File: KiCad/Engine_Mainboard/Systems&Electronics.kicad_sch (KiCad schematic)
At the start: 50 parts, among them J1 Pressure Transducer, J12 Screw_Terminal_01x02, J13 Screw_Terminal_01x03, J2 Pressure Transducer, J3 Pressure Transducer, J4 Pressure Transducer, J5 Pressure Transducer, J6 Pressure Transducer

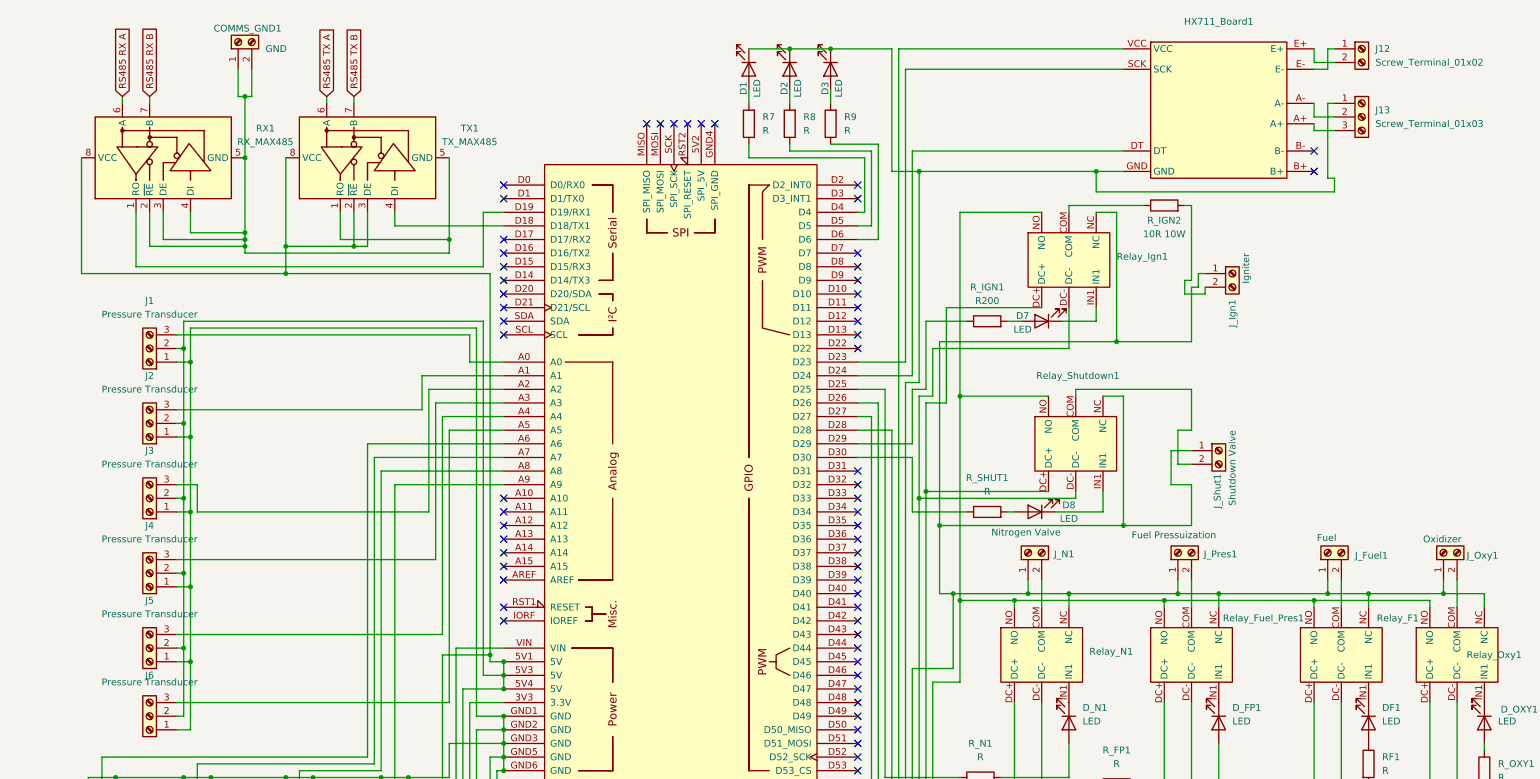
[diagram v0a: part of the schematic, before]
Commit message: PCB design reorg
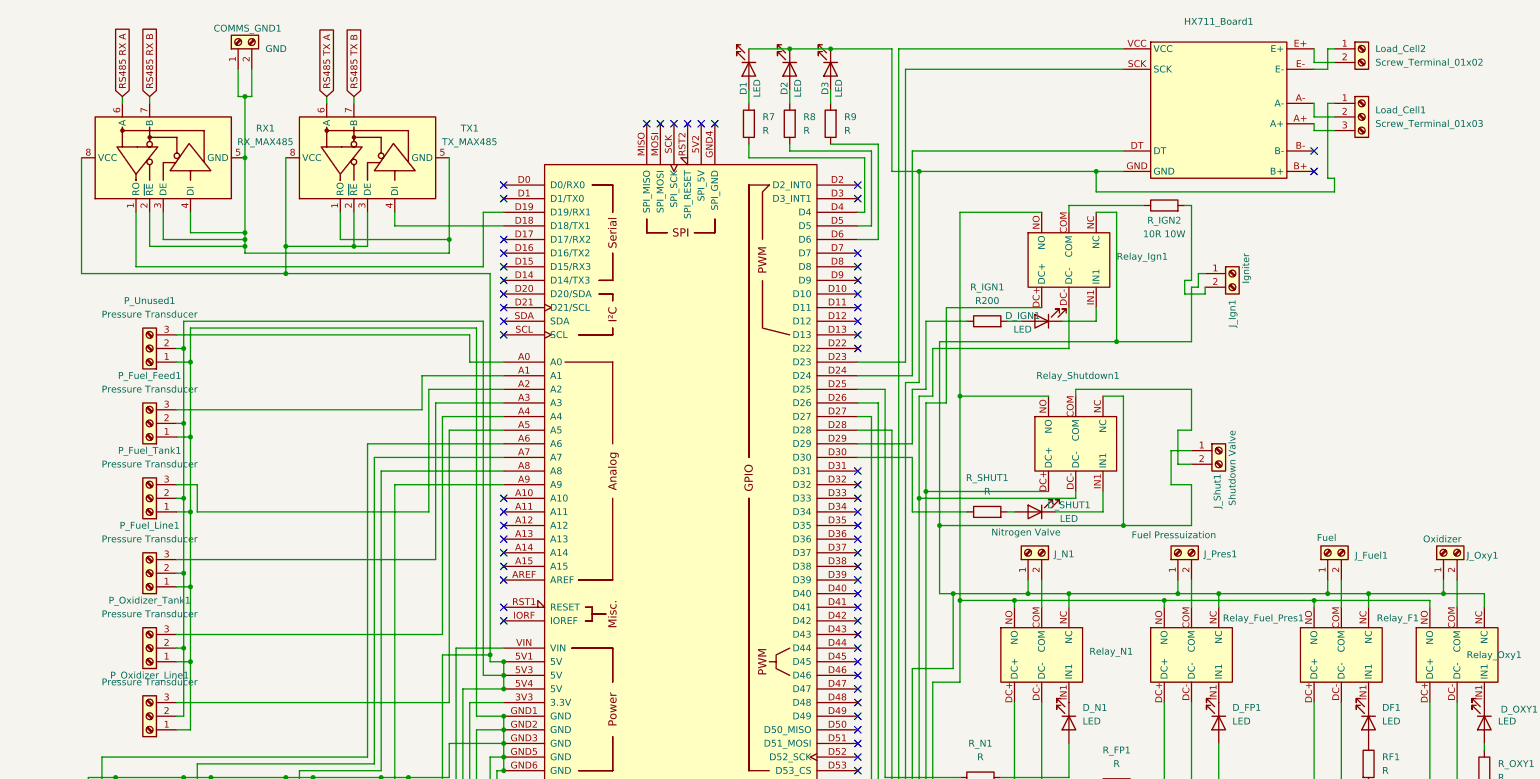
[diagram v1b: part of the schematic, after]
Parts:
- renumbered D7 to D_IGN1, D8 to D_SHUT1, J13 to Load_Cell1, J12 to Load_Cell2, J2 to P_Fuel_Feed1, J4 to P_Fuel_Line1, J3 to P_Fuel_Tank1, J6 to P_Oxidizer_Line1, J5 to P_Oxidizer_Tank1, J1 to P_Unused1
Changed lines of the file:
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@@
 		(on_board yes)
 		(dnp no)
-		(property "Reference" "J6"
+		(property "Reference" "P_Oxidizer_Line1"
 			(at 27.94 135.89 0)
 			(effects
@@
 			(project "Systems&Electronics"
 				(path "/4e05caf8-77e4-4a22-9a05-51fcca8e50ff"
-					(reference "J6")
+					(reference "P_Oxidizer_Line1")
 					(unit 1)
 				)
@@
 		(dnp no)
 		(fields_autoplaced yes)
-		(property "Reference" "J4"
+		(property "Reference" "P_Fuel_Line1"
 			(at 27.94 107.95 0)
 			(effects
@@
 			(project "Systems&Electronics"
 				(path "/4e05caf8-77e4-4a22-9a05-51fcca8e50ff"
-					(reference "J4")
+					(reference "P_Fuel_Line1")
 					(unit 1)
 				)
@@
 		(dnp no)
 		(fields_autoplaced yes)
-		(property "Reference" "J3"
+		(property "Reference" "P_Fuel_Tank1"
 			(at 27.94 93.98 0)
 			(effects
@@
 			(project "Systems&Electronics"
 				(path "/4e05caf8-77e4-4a22-9a05-51fcca8e50ff"
-					(reference "J3")
+					(reference "P_Fuel_Tank1")
 					(unit 1)
 				)
@@
 		(on_board yes)
 		(dnp no)
-		(property "Reference" "D8"
+		(property "Reference" "D_SHUT1"
 			(at 199.39 104.14 0)
 			(effects
@@
 			(project "Systems&Electronics"
 				(path "/4e05caf8-77e4-4a22-9a05-51fcca8e50ff"
-					(reference "D8")
+					(reference "D_SHUT1")
 					(unit 1)
 				)
@@
 	)
 	(symbol
+		(lib_name "Sensors:AD8495_PCB")
 		(lib_id "Sensors:AD8495_PCB")
 		(at 57.15 168.91 180)
@@
 	)
 	(symbol
+		(lib_name "Sensors:AD8495_PCB")
 		(lib_id "Sensors:AD8495_PCB")
 		(at 74.93 168.91 180)
@@
 		(dnp no)
 		(fields_autoplaced yes)
-		(property "Reference" "J2"
+		(property "Reference" "P_Fuel_Feed1"
 			(at 27.94 80.01 0)
 			(effects
@@
 			(project ""
 				(path "/4e05caf8-77e4-4a22-9a05-51fcca8e50ff"
-					(reference "J2")
+					(reference "P_Fuel_Feed1")
 					(unit 1)
 				)
@@
 		(dnp no)
 		(fields_autoplaced yes)
-		(property "Reference" "J12"
+		(property "Reference" "Load_Cell2"
 			(at 256.54 19.0499 0)
 			(effects
@@
 			(project ""
 				(path "/4e05caf8-77e4-4a22-9a05-51fcca8e50ff"
-					(reference "J12")
+					(reference "Load_Cell2")
 					(unit 1)
 				)
@@
 		(dnp no)
 		(fields_autoplaced yes)
-		(property "Reference" "J1"
+		(property "Reference" "P_Unused1"
 			(at 27.94 66.04 0)
 			(effects
@@
 			(project "Systems&Electronics"
 				(path "/4e05caf8-77e4-4a22-9a05-51fcca8e50ff"
-					(reference "J1")
+					(reference "P_Unused1")
 					(unit 1)
 				)
@@
 	)
 	(symbol
+		(lib_name "Sensors:AD8495_PCB")
 		(lib_id "Sensors:AD8495_PCB")
 		(at 38.1 168.91 180)
@@
 		(dnp no)
 		(fields_autoplaced yes)
-		(property "Reference" "J13"
+		(property "Reference" "Load_Cell1"
 			(at 256.54 30.4799 0)
 			(effects
@@
 			(project ""
 				(path "/4e05caf8-77e4-4a22-9a05-51fcca8e50ff"
-					(reference "J13")
+					(reference "Load_Cell1")
 					(unit 1)
 				)
@@
 		(dnp no)
 		(fields_autoplaced yes)
-		(property "Reference" "J5"
+		(property "Reference" "P_Oxidizer_Tank1"
 			(at 27.94 121.92 0)
 			(effects
@@
 			(project "Systems&Electronics"
 				(path "/4e05caf8-77e4-4a22-9a05-51fcca8e50ff"
-					(reference "J5")
+					(reference "P_Oxidizer_Tank1")
 					(unit 1)
 				)
@@
 	)
 	(symbol
+		(lib_name "Sensors:AD8495_PCB")
 		(lib_id "Sensors:AD8495_PCB")
 		(at 20.32 168.91 180)
@@
 		(on_board yes)
 		(dnp no)
-		(property "Reference" "D7"
+		(property "Reference" "D_IGN1"
 			(at 190.754 68.834 0)
 			(effects
@@
 			(project "Systems&Electronics"
 				(path "/4e05caf8-77e4-4a22-9a05-51fcca8e50ff"
-					(reference "D7")
+					(reference "D_IGN1")
 					(unit 1)
 				)

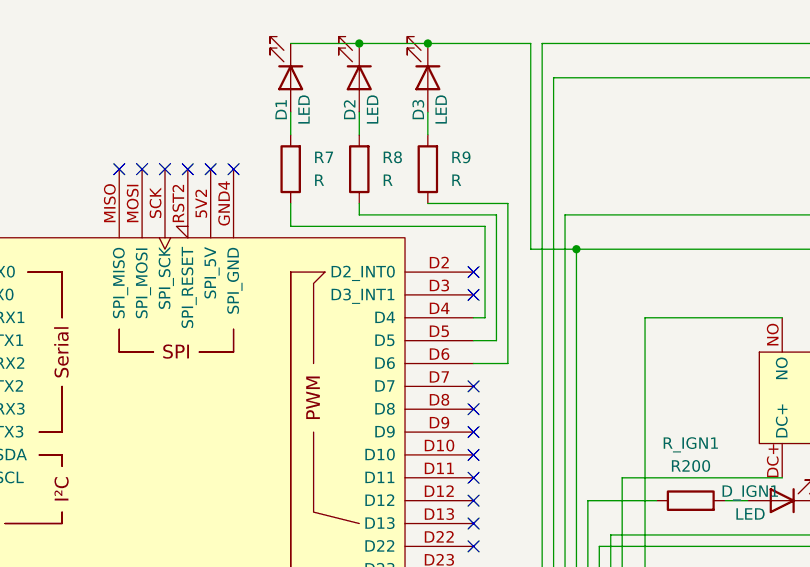
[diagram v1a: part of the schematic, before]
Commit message: PCB Ignition Resistor Move
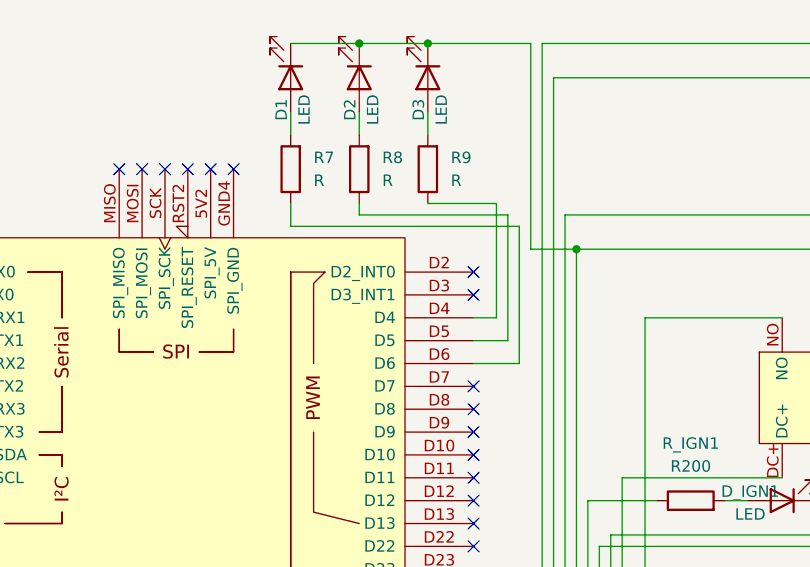
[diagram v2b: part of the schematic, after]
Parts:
- D1, D2, D3, DF1, D_FP1, D_IGN1, D_N1, D_OXY1, D_SHUT1: footprint LED_THT:LED_D3.0mm -> LED_THT:LED_D5.0mm
- R7, R8, R9, RF1, R_FP1, R_IGN1, R_N1, R_OXY1, R_SHUT1: footprint Resistor_THT:R_Axial_DIN0204_L3.6mm_D1.6mm_P5.08mm_Horizontal -> Resistor_THT:R_Axial_DIN0207_L6.3mm_D2.5mm_P7.62mm_Horizontal
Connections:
- net at R9.1: now also A1.D4; no longer A1.D6
- net at R7.1: now also A1.D6; no longer A1.D4
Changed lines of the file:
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@@
 	(wire
 		(pts
+			(xy 163.83 38.1) (xy 163.83 52.07)
+		)
+		(stroke
+			(width 0)
+			(type default)
+		)
+	)
+	(wire
+		(pts
 			(xy 36.83 152.4) (xy 36.83 160.02)
 		)
@@
 	(wire
 		(pts
-			(xy 161.29 39.37) (xy 161.29 49.53)
-		)
-		(stroke
-			(width 0)
-			(type default)
-		)
-	)
-	(wire
-		(pts
 			(xy 199.39 148.59) (xy 199.39 154.94)
 		)
@@
 	(wire
 		(pts
-			(xy 160.02 52.07) (xy 162.56 52.07)
+			(xy 160.02 52.07) (xy 163.83 52.07)
 		)
 		(stroke
@@
 	(wire
 		(pts
-			(xy 162.56 38.1) (xy 147.32 38.1)
+			(xy 147.32 38.1) (xy 163.83 38.1)
 		)
 		(stroke
@@
 	(wire
 		(pts
-			(xy 163.83 54.61) (xy 163.83 36.83)
-		)
-		(stroke
-			(width 0)
-			(type default)
-		)
-	)
-	(wire
-		(pts
 			(xy 208.28 49.53) (xy 208.28 73.66)
 		)
@@
 	(wire
 		(pts
+			(xy 162.56 36.83) (xy 162.56 49.53)
+		)
+		(stroke
+			(width 0)
+			(type default)
+		)
+	)
+	(wire
+		(pts
 			(xy 53.34 39.37) (xy 53.34 55.88)
 		)
@@
 	(wire
 		(pts
-			(xy 160.02 54.61) (xy 163.83 54.61)
+			(xy 160.02 54.61) (xy 165.1 54.61)
 		)
 		(stroke
@@
 	(wire
 		(pts
+			(xy 162.56 36.83) (xy 154.94 36.83)
+		)
+		(stroke
+			(width 0)
+			(type default)
+		)
+	)
+	(wire
+		(pts
 			(xy 90.17 135.89) (xy 93.98 135.89)
 		)
@@
 	(wire
 		(pts
-			(xy 162.56 52.07) (xy 162.56 38.1)
-		)
-		(stroke
-			(width 0)
-			(type default)
-		)
-	)
-	(wire
-		(pts
 			(xy 250.19 118.11) (xy 250.19 123.19)
 		)
@@
 	(wire
 		(pts
-			(xy 160.02 49.53) (xy 161.29 49.53)
+			(xy 160.02 49.53) (xy 162.56 49.53)
 		)
 		(stroke
@@
 	(wire
 		(pts
-			(xy 163.83 36.83) (xy 154.94 36.83)
-		)
-		(stroke
-			(width 0)
-			(type default)
-		)
-	)
-	(wire
-		(pts
 			(xy 147.32 19.05) (xy 154.94 19.05)
 		)
@@
 	(wire
 		(pts
-			(xy 161.29 39.37) (xy 139.7 39.37)
+			(xy 139.7 39.37) (xy 165.1 39.37)
 		)
 		(stroke
@@
 	(wire
 		(pts
+			(xy 165.1 39.37) (xy 165.1 54.61)
+		)
+		(stroke
+			(width 0)
+			(type default)
+		)
+	)
+	(wire
+		(pts
 			(xy 179.07 121.92) (xy 189.23 121.92)
 		)
@@
 			)
 		)
-		(property "Footprint" "Resistor_THT:R_Axial_DIN0204_L3.6mm_D1.6mm_P5.08mm_Horizontal"
+		(property "Footprint" "Resistor_THT:R_Axial_DIN0207_L6.3mm_D2.5mm_P7.62mm_Horizontal"
 			(at 184.15 71.628 90)
 			(effects
@@
 			)
 		)
-		(property "Footprint" "Resistor_THT:R_Axial_DIN0204_L3.6mm_D1.6mm_P5.08mm_Horizontal"
+		(property "Footprint" "Resistor_THT:R_Axial_DIN0207_L6.3mm_D2.5mm_P7.62mm_Horizontal"
 			(at 253.492 152.4 90)
 			(effects
@@
 			)
 		)
-		(property "Footprint" "LED_THT:LED_D3.0mm"
+		(property "Footprint" "LED_THT:LED_D5.0mm"
 			(at 227.33 144.78 0)
 			(effects
@@
 			)
 		)
-		(property "Footprint" "Resistor_THT:R_Axial_DIN0204_L3.6mm_D1.6mm_P5.08mm_Horizontal"
+		(property "Footprint" "Resistor_THT:R_Axial_DIN0207_L6.3mm_D2.5mm_P7.62mm_Horizontal"
 			(at 184.15 107.188 90)
 			(effects
@@
 			)
 		)
-		(property "Footprint" "LED_THT:LED_D3.0mm"
+		(property "Footprint" "LED_THT:LED_D5.0mm"
 			(at 193.04 105.41 0)
 			(effects
@@
 			)
 		)
-		(property "Footprint" "LED_THT:LED_D3.0mm"
+		(property "Footprint" "LED_THT:LED_D5.0mm"
 			(at 139.7 22.86 0)
 			(effects
@@
 	)
 	(symbol
-		(lib_name "Sensors:AD8495_PCB")
 		(lib_id "Sensors:AD8495_PCB")
 		(at 57.15 168.91 180)
@@
 			)
 		)
-		(property "Footprint" "LED_THT:LED_D3.0mm"
+		(property "Footprint" "LED_THT:LED_D5.0mm"
 			(at 199.39 144.78 0)
 			(effects
@@
 	)
 	(symbol
-		(lib_name "Sensors:AD8495_PCB")
 		(lib_id "Sensors:AD8495_PCB")
 		(at 74.93 168.91 180)
@@
 			)
 		)
-		(property "Footprint" "LED_THT:LED_D3.0mm"
+		(property "Footprint" "LED_THT:LED_D5.0mm"
 			(at 147.32 22.86 0)
 			(effects
@@
 			)
 		)
-		(property "Footprint" "Resistor_THT:R_Axial_DIN0204_L3.6mm_D1.6mm_P5.08mm_Horizontal"
+		(property "Footprint" "Resistor_THT:R_Axial_DIN0207_L6.3mm_D2.5mm_P7.62mm_Horizontal"
 			(at 156.718 33.02 90)
 			(effects
@@
 			)
 		)
-		(property "Footprint" "LED_THT:LED_D3.0mm"
+		(property "Footprint" "LED_THT:LED_D5.0mm"
 			(at 154.94 22.86 0)
 			(effects
@@
 	)
 	(symbol
-		(lib_name "Sensors:AD8495_PCB")
 		(lib_id "Sensors:AD8495_PCB")
 		(at 38.1 168.91 180)
@@
 			)
 		)
-		(property "Footprint" "Resistor_THT:R_Axial_DIN0204_L3.6mm_D1.6mm_P5.08mm_Horizontal"
+		(property "Footprint" "Resistor_THT:R_Axial_DIN0207_L6.3mm_D2.5mm_P7.62mm_Horizontal"
 			(at 208.28 157.988 90)
 			(effects
@@
 			)
 		)
-		(property "Footprint" "Resistor_THT:R_Axial_DIN0204_L3.6mm_D1.6mm_P5.08mm_Horizontal"
+		(property "Footprint" "Resistor_THT:R_Axial_DIN0207_L6.3mm_D2.5mm_P7.62mm_Horizontal"
 			(at 149.098 33.02 90)
 			(effects
@@
 			)
 		)
-		(property "Footprint" "LED_THT:LED_D3.0mm"
+		(property "Footprint" "LED_THT:LED_D5.0mm"
 			(at 276.86 144.78 0)
 			(effects
@@
 			)
 		)
-		(property "Footprint" "LED_THT:LED_D3.0mm"
+		(property "Footprint" "LED_THT:LED_D5.0mm"
 			(at 255.27 144.78 0)
 			(effects
@@
 			)
 		)
-		(property "Footprint" "Resistor_THT:R_Axial_DIN0204_L3.6mm_D1.6mm_P5.08mm_Horizontal"
+		(property "Footprint" "Resistor_THT:R_Axial_DIN0207_L6.3mm_D2.5mm_P7.62mm_Horizontal"
 			(at 141.478 33.02 90)
 			(effects
@@
 			)
 		)
-		(property "Footprint" "Resistor_THT:R_Axial_DIN0204_L3.6mm_D1.6mm_P5.08mm_Horizontal"
+		(property "Footprint" "Resistor_THT:R_Axial_DIN0207_L6.3mm_D2.5mm_P7.62mm_Horizontal"
 			(at 182.88 156.718 90)
 			(effects
@@
 	)
 	(symbol
-		(lib_name "Sensors:AD8495_PCB")
 		(lib_id "Sensors:AD8495_PCB")
 		(at 20.32 168.91 180)
@@
 			)
 		)
-		(property "Footprint" "LED_THT:LED_D3.0mm"
+		(property "Footprint" "LED_THT:LED_D5.0mm"
 			(at 194.31 69.85 0)
 			(effects
@@
 			)
 		)
-		(property "Footprint" "Resistor_THT:R_Axial_DIN0204_L3.6mm_D1.6mm_P5.08mm_Horizontal"
+		(property "Footprint" "Resistor_THT:R_Axial_DIN0207_L6.3mm_D2.5mm_P7.62mm_Horizontal"
 			(at 275.082 153.67 90)
 			(effects
